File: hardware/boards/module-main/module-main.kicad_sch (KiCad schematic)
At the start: 2 parts, among them J2 2x10 2.54mm pin header, J3 Neutrik NE8FAV

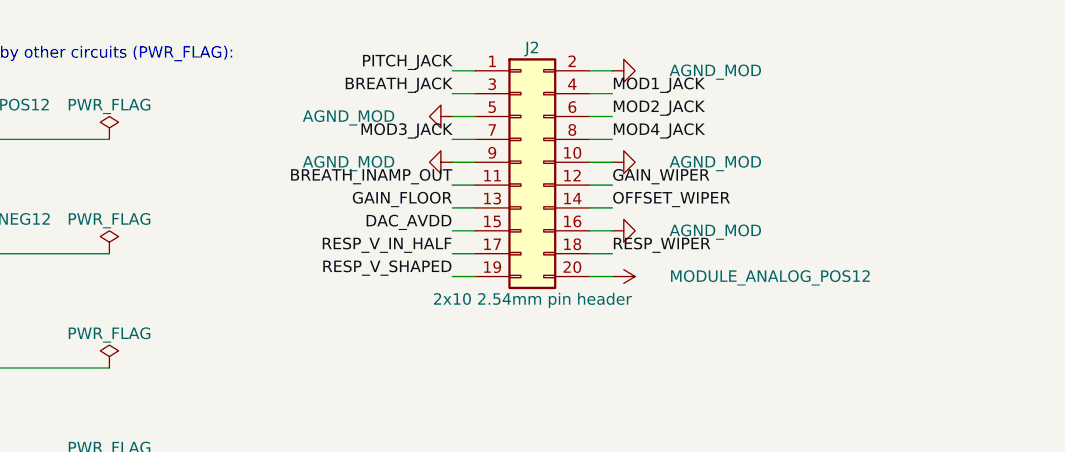
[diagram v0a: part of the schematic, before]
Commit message: Module schematics: the ten circuits' netlists exported from their sheets; J-B2B-MOD allocated by position
- Every module circuit's netlist.yaml is now EXPORTED from its KiCad sheet
  (ADR 0019), identical part by part and net by net to the hand-written one,
  including its foreign: parts. kicad.py exports foreign: from FOREIGN lines of
  sheet text; without it the breath receive page's R1 went unresolved.
- J-B2B-MOD, re-allocated: the pots' nets on the top rows (the pots sit above
  the header), each side's pot and jacks in its own column, a ground on the
  diagonal of every other row so every signal but the LED's +12 V has a ground
  pin beside it.
- kicad.py check: J-B2B-MOD is one conductor per pin on both module boards, and
  the main board's etherCON matches hardware/interfaces/spi-link pin for pin.
- sch.py: a board's sub-sheet pin with one member is a no-connect again (the
  interfaces' spare-label rule assumed a part pin).

Co-Authored-By: Claude Opus 5.5 <noreply@anthropic.com>
Claude-Session: https://claude.ai/code/session_01LmB4muFXnoLprWX4JzuJ5A
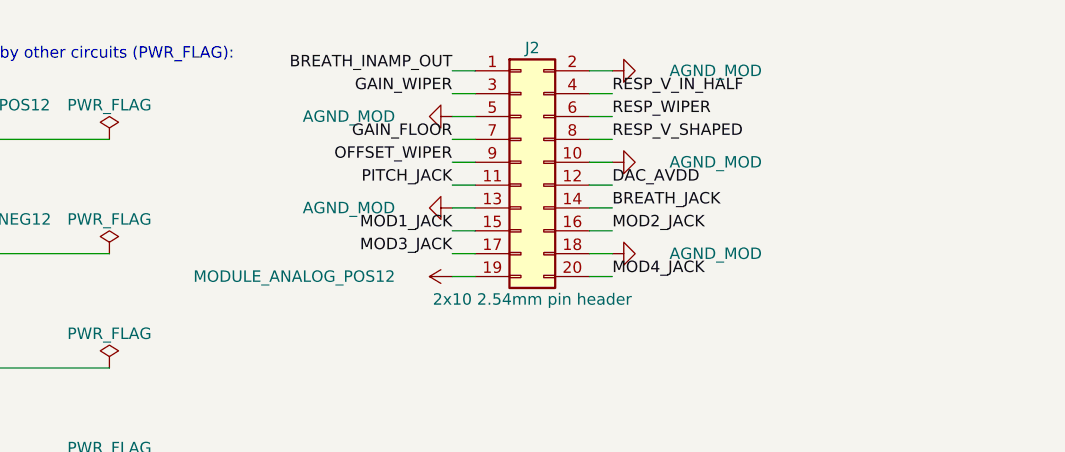
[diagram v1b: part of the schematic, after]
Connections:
- net AGND_MOD: now also J2.13 (Pin_13), J2.18 (Pin_18); no longer J2.16 (Pin_16), J2.9 (Pin_9)
- net BREATH_INAMP_OUT: now also J2.1 (Pin_1); no longer J2.11 (Pin_11)
- net BREATH_JACK: now also J2.14 (Pin_14); no longer J2.3 (Pin_3)
- net DAC_AVDD: now also J2.12 (Pin_12); no longer J2.15 (Pin_15)
- net GAIN_FLOOR: now also J2.7 (Pin_7); no longer J2.13 (Pin_13)
- net GAIN_WIPER: now also J2.3 (Pin_3); no longer J2.12 (Pin_12)
- net MOD1_JACK: now also J2.15 (Pin_15); no longer J2.4 (Pin_4)
- net MOD2_JACK: now also J2.16 (Pin_16); no longer J2.6 (Pin_6)
- net MOD3_JACK: now also J2.17 (Pin_17); no longer J2.7 (Pin_7)
- net MOD4_JACK: now also J2.20 (Pin_20); no longer J2.8 (Pin_8)
- net MODULE_ANALOG_POS12: now also J2.19 (Pin_19); no longer J2.20 (Pin_20)
- net OFFSET_WIPER: now also J2.9 (Pin_9); no longer J2.14 (Pin_14)
- net PITCH_JACK: now also J2.11 (Pin_11); no longer J2.1 (Pin_1)
- net RESP_V_IN_HALF: now also J2.4 (Pin_4); no longer J2.17 (Pin_17)
- net RESP_V_SHAPED: now also J2.8 (Pin_8); no longer J2.19 (Pin_19)
- net RESP_WIPER: now also J2.6 (Pin_6); no longer J2.18 (Pin_18)

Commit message: dac8568: CLR is a net inside the circuit, tied inactive, not a port waiting for an unfitted part
CLR is active low and falling-edge triggered (SBAS430E p.40); R-CLR-PU ties it
to AVDD and LK-CLR asserts it by hand. The hierarchical port, the board's
no-connect sheet pin and the nets.yaml boundary entry are gone. Whether to
restore link supervision is marked as the owner's decision.

Co-Authored-By: Claude Opus 5.5 <noreply@anthropic.com>
Claude-Session: https://claude.ai/code/session_01LmB4muFXnoLprWX4JzuJ5A
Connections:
- no-connect marks 1 -> 0
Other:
- sheet dac8568 ports: added none; removed CLR
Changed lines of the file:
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@@
     (instances (project "module-main" (path "/fc77e9f9-9171-5c83-92ae-8cafe880764e" (reference "#PWR35") (unit 1))))
   )
-  (no_connect (at 457.2 55.88))
   (wire (pts (xy 457.2 58.42) (xy 454.66 58.42)) (stroke (width 0) (type default)))
   (label "SCLK_DAC" (at 454.66 58.42 180) (fields_autoplaced) (effects (font (size 1.27 1.27)) (justify right bottom)))
@@
     (property "Sheetfile" "../../module/dac8568/dac8568.kicad_sch" (at 457.2 73.66 0) (effects (font (size 1.27 1.27)) (justify left top)))
     (pin "DAC_AVDD" input (at 457.2 53.34 180) (effects (font (size 1.27 1.27)) (justify left)))
-    (pin "CLR" input (at 457.2 55.88 180) (effects (font (size 1.27 1.27)) (justify left)))
     (pin "SCLK_DAC" input (at 457.2 58.42 180) (effects (font (size 1.27 1.27)) (justify left)))
     (pin "DIN" input (at 457.2 60.96 180) (effects (font (size 1.27 1.27)) (justify left)))

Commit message: Panel LED hangs on the load switch output: lit = delivering, dark = off or latched
The LED was on the analog +12 V rail, live whenever the rack is, so it could
not show the -1's latch - the one thing it was kept for. The banked LT1641
datasheet shows TIMER and GATE hold no 'latched' level and PWRGD has the wrong
sense; the output does. J-B2B-MOD pin 19 carries UMBILICAL_POS12 on both
boards; nets.yaml and the allocation table follow.

Co-Authored-By: Claude Opus 5.5 <noreply@anthropic.com>
Claude-Session: https://claude.ai/code/session_01LmB4muFXnoLprWX4JzuJ5A
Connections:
- net MODULE_ANALOG_POS12: no longer J2.19 (Pin_19)
- net UMBILICAL_POS12: now also J2.19 (Pin_19)
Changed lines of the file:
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@@
   (label "MOD3_JACK" (at 454.66 165.1 180) (fields_autoplaced) (effects (font (size 1.27 1.27)) (justify right bottom)))
   (wire (pts (xy 101.6 76.2) (xy 99.06 76.2)) (stroke (width 0) (type default)))
-  (symbol (lib_id "power:+12V") (at 99.06 76.2 90) (unit 1)
-    (in_bom yes) (on_board yes) (dnp no)
-    (property "Reference" "#PWR13" (at 102.87 76.2 0) (effects (font (size 1.27 1.27)) hide))
-    (property "Value" "MODULE_ANALOG_POS12" (at 92.71 76.2 90) (effects (font (size 1.27 1.27)) (justify left)))
-    (property "Footprint" "" (at 99.06 76.2 0) (effects (font (size 1.27 1.27)) hide))
-    (property "Datasheet" "" (at 99.06 76.2 0) (effects (font (size 1.27 1.27)) hide))
-    (pin "1")
-    (instances (project "module-main" (path "/fc77e9f9-9171-5c83-92ae-8cafe880764e" (reference "#PWR13") (unit 1))))
-  )
+  (label "UMBILICAL_POS12" (at 99.06 76.2 180) (fields_autoplaced) (effects (font (size 1.27 1.27)) (justify right bottom)))
   (wire (pts (xy 254.0 55.88) (xy 256.54 55.88)) (stroke (width 0) (type default)))
   (symbol (lib_id "power:+12V") (at 256.54 55.88 270) (unit 1)

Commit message: Breath response shaper adopted: restoring half drawn, output feeds POT-GAIN; pots ordered to fit the knob
U-RESP B restores x2 inverting (R-RESTORE-IN 10k, R-RESTORE-FB 20k): unity and
the in-amp's polarity at centre detent. BREATH_SHAPED feeds POT-GAIN on
J-B2B-MOD pin 1; nets.yaml moves the shaper from proposed to fitted.
POT-GAIN linear (the design's working gain sits at noon); POT-OFFSET gets no
detent. POT-GAIN/OFFSET are Song Huei R0904N KC (18-tooth, the T18 knob's
shaft; KQ is 40-tooth); POT-RESP Alpha RV09AF-40-25B-B50K-0C (18-tooth B shaft,
centre click). POT-OFFSET's zero is +18.7 deg on the 280-deg track, not 300.

Co-Authored-By: Claude Opus 5.5 <noreply@anthropic.com>
Claude-Session: https://claude.ai/code/session_01LmB4muFXnoLprWX4JzuJ5A
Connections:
- net BREATH_INAMP_OUT: no longer J2.1 (Pin_1)
- new net BREATH_SHAPED: J2.1 (Pin_1)
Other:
- sheet breath-response-shaper ports: added BREATH_SHAPED; removed none
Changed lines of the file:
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@@
   )
   (wire (pts (xy 101.6 53.34) (xy 99.06 53.34)) (stroke (width 0) (type default)))
-  (label "BREATH_INAMP_OUT" (at 99.06 53.34 180) (fields_autoplaced) (effects (font (size 1.27 1.27)) (justify right bottom)))
+  (label "BREATH_SHAPED" (at 99.06 53.34 180) (fields_autoplaced) (effects (font (size 1.27 1.27)) (justify right bottom)))
   (wire (pts (xy 254.0 96.52) (xy 256.54 96.52)) (stroke (width 0) (type default)))
   (label "BREATH_INAMP_OUT" (at 256.54 96.52 0) (fields_autoplaced) (effects (font (size 1.27 1.27)) (justify left bottom)))
@@
     (pin "MODULE_ANALOG_NEG12" input (at 330.2 147.32 180) (effects (font (size 1.27 1.27)) (justify left)))
     (pin "V_SHAPED" passive (at 330.2 149.86 180) (effects (font (size 1.27 1.27)) (justify left)))
+    (pin "BREATH_SHAPED" output (at 330.2 152.4 180) (effects (font (size 1.27 1.27)) (justify left)))
     (instances (project "module-main" (path "/fc77e9f9-9171-5c83-92ae-8cafe880764e" (page "8"))))
   )
+  (wire (pts (xy 330.2 152.4) (xy 327.66 152.4)) (stroke (width 0) (type default)))
+  (label "BREATH_SHAPED" (at 327.66 152.4 180) (fields_autoplaced) (effects (font (size 1.27 1.27)) (justify right bottom)))
   (sheet (at 203.2 139.7) (size 50.8 20.32) (exclude_from_sim no) (in_bom yes) (on_board yes) (dnp no)
     (stroke (width 0.1524) (type solid)) (fill (color 0 0 0 0.0000))

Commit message: Module: four-layer ground settled, local 5 V, metal standoffs, pitch budget, board-to-board header
Owner decisions of 2026-09-30 applied. dig-gnd-topology settled: one star at
J-PWR-EURO's ground pins, DIG_GND a layer-2 plane tied there by the new
NT-DIG-MOD, AGND_MOD its own region by NT-AGND-MOD, PWR_GND on layer 4; the
proposal's bridge under the DAC dropped per SBAS430E p.49 (DIG_GND was an
island tied only through the cable before). PCB-MODULE four layers, the jack
board two. The bus +5 V is not used: U-REG-LOGIC (ADP7118AUJZ-5.0, banked)
makes LOGIC_5V from the analog +12 V; FB4/C4 gone, the 16-pin header kept
with its +5 V/CV/Gate pins no-connect (ADR 0023 point 3 amended). Metal
standoffs: pads AGND_MOD on the jack board, no net on the main board.
pitch-cents-budget settled at 0.76 cents linear / 0.45 RSS from one table.
J-B2B-MOD is Samtec TSW-110-09-G-D. Module sims are stale and re-run next.

Co-Authored-By: Claude Opus 5.5 <noreply@anthropic.com>
Claude-Session: https://claude.ai/code/session_01LmB4muFXnoLprWX4JzuJ5A
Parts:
- J2: LCSC (none) -> C7366478; MPN (none) -> TSW-110-09-G-D; Manufacturer (none) -> Samtec
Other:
- sheet digital-and-supervision ports: added LOGIC_5V; removed BUS_5V
- sheet power-entry ports: added LOGIC_5V; removed BUS_5V
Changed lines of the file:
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@@
     (property "Note" "Soldered through both module boards, no mated contact (ADR 0023). Its pin k is the same conductor on both boards; tools/kicad.py check holds the two sheets to that. Allocation and reasoning: hardware/boards/module-main/README.md" (at 106.68 63.5 0) (effects (font (size 1.27 1.27)) hide))
     (property "Pins_source" "header position n on pin n, odd/even across the two rows as a 2x10 header numbers them" (at 106.68 63.5 0) (effects (font (size 1.27 1.27)) hide))
-    (property "Manufacturer" "" (at 106.68 63.5 0) (effects (font (size 1.27 1.27)) hide))
-    (property "MPN" "" (at 106.68 63.5 0) (effects (font (size 1.27 1.27)) hide))
-    (property "LCSC" "" (at 106.68 63.5 0) (effects (font (size 1.27 1.27)) hide))
+    (property "Manufacturer" "Samtec" (at 106.68 63.5 0) (effects (font (size 1.27 1.27)) hide))
+    (property "MPN" "TSW-110-09-G-D" (at 106.68 63.5 0) (effects (font (size 1.27 1.27)) hide))
+    (property "LCSC" "C7366478" (at 106.68 63.5 0) (effects (font (size 1.27 1.27)) hide))
     (property "Assembly" "hand" (at 106.68 63.5 0) (effects (font (size 1.27 1.27)) hide))
     (pin "1")
@@
     (in_bom yes) (on_board yes) (dnp no)
     (property "Reference" "#PWR34" (at 252.73 60.96 0) (effects (font (size 1.27 1.27)) hide))
-    (property "Value" "BUS_5V" (at 262.89 60.96 270) (effects (font (size 1.27 1.27)) (justify right)))
+    (property "Value" "LOGIC_5V" (at 262.89 60.96 270) (effects (font (size 1.27 1.27)) (justify right)))
     (property "Footprint" "" (at 256.54 60.96 0) (effects (font (size 1.27 1.27)) hide))
     (property "Datasheet" "" (at 256.54 60.96 0) (effects (font (size 1.27 1.27)) hide))
@@
     (in_bom yes) (on_board yes) (dnp no)
     (property "Reference" "#PWR35" (at 331.47 96.52 0) (effects (font (size 1.27 1.27)) hide))
-    (property "Value" "BUS_5V" (at 321.31 96.52 90) (effects (font (size 1.27 1.27)) (justify left)))
+    (property "Value" "LOGIC_5V" (at 321.31 96.52 90) (effects (font (size 1.27 1.27)) (justify left)))
     (property "Footprint" "" (at 327.66 96.52 0) (effects (font (size 1.27 1.27)) hide))
     (property "Datasheet" "" (at 327.66 96.52 0) (effects (font (size 1.27 1.27)) hide))
@@
     (instances (project "module-main" (path "/fc77e9f9-9171-5c83-92ae-8cafe880764e" (reference "#FLG45") (unit 1))))
   )
-  (symbol (lib_id "power:+5V") (at 43.18 124.46 0) (unit 1)
-    (in_bom yes) (on_board yes) (dnp no)
-    (property "Reference" "#PWR46" (at 43.18 128.27 0) (effects (font (size 1.27 1.27)) hide))
-    (property "Value" "BUS_5V" (at 43.18 120.65 0) (effects (font (size 1.27 1.27))))
-    (property "Footprint" "" (at 43.18 124.46 0) (effects (font (size 1.27 1.27)) hide))
-    (property "Datasheet" "" (at 43.18 124.46 0) (effects (font (size 1.27 1.27)) hide))
-    (pin "1")
-    (instances (project "module-main" (path "/fc77e9f9-9171-5c83-92ae-8cafe880764e" (reference "#PWR46") (unit 1))))
-  )
-  (wire (pts (xy 43.18 124.46) (xy 60.96 124.46)) (stroke (width 0) (type default)))
-  (symbol (lib_id "power:PWR_FLAG") (at 60.96 124.46 0) (unit 1)
-    (in_bom yes) (on_board yes) (dnp no)
-    (property "Reference" "#FLG47" (at 60.96 121.92 0) (effects (font (size 1.27 1.27)) hide))
-    (property "Value" "PWR_FLAG" (at 60.96 120.65 0) (effects (font (size 1.27 1.27))))
-    (property "Footprint" "" (at 60.96 124.46 0) (effects (font (size 1.27 1.27)) hide))
-    (property "Datasheet" "" (at 60.96 124.46 0) (effects (font (size 1.27 1.27)) hide))
-    (pin "1")
-    (instances (project "module-main" (path "/fc77e9f9-9171-5c83-92ae-8cafe880764e" (reference "#FLG47") (unit 1))))
-  )
   (symbol (lib_id "power:+12V") (at 43.18 137.16 0) (unit 1)
     (in_bom yes) (on_board yes) (dnp no)
@@
     (pin "MODULE_ANALOG_POS12" output (at 254.0 55.88 0) (effects (font (size 1.27 1.27)) (justify right)))
     (pin "MODULE_ANALOG_NEG12" output (at 254.0 58.42 0) (effects (font (size 1.27 1.27)) (justify right)))
-    (pin "BUS_5V" output (at 254.0 60.96 0) (effects (font (size 1.27 1.27)) (justify right)))
+    (pin "LOGIC_5V" output (at 254.0 60.96 0) (effects (font (size 1.27 1.27)) (justify right)))
     (pin "DAC_AVDD" output (at 254.0 63.5 0) (effects (font (size 1.27 1.27)) (justify right)))
     (instances (project "module-main" (path "/fc77e9f9-9171-5c83-92ae-8cafe880764e" (page "2"))))
@@
     (pin "MOSI" input (at 330.2 91.44 180) (effects (font (size 1.27 1.27)) (justify left)))
     (pin "CS_MOD" input (at 330.2 93.98 180) (effects (font (size 1.27 1.27)) (justify left)))
-    (pin "BUS_5V" input (at 330.2 96.52 180) (effects (font (size 1.27 1.27)) (justify left)))
+    (pin "LOGIC_5V" input (at 330.2 96.52 180) (effects (font (size 1.27 1.27)) (justify left)))
     (pin "DAC_AVDD" input (at 330.2 99.06 180) (effects (font (size 1.27 1.27)) (justify left)))
     (pin "DIG_GND" passive (at 330.2 101.6 180) (effects (font (size 1.27 1.27)) (justify left)))

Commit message: WIP module power entry: rail PTCs, the instrument's isolated supply (U-ISO), ground split
Sheets, exports, BOM rows, banked datasheets (manifest fragment to follow).
The page drawing, ADR 0027, figures and sims are the next commits.

Co-Authored-By: Claude Opus 5.5 <noreply@anthropic.com>
Claude-Session: https://claude.ai/code/session_01LmB4muFXnoLprWX4JzuJ5A
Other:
- sheet power-entry ports: added ISO_POS12; removed BUS_POS12_RAW
- sheet umbilical-load-switch ports: added ISO_POS12; removed BUS_POS12_RAW
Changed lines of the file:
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@@
     (in_bom yes) (on_board yes) (dnp no)
     (property "Reference" "#PWR26" (at 252.73 53.34 0) (effects (font (size 1.27 1.27)) hide))
-    (property "Value" "BUS_POS12_RAW" (at 262.89 53.34 270) (effects (font (size 1.27 1.27)) (justify right)))
+    (property "Value" "ISO_POS12" (at 262.89 53.34 270) (effects (font (size 1.27 1.27)) (justify right)))
     (property "Footprint" "" (at 256.54 53.34 0) (effects (font (size 1.27 1.27)) hide))
     (property "Datasheet" "" (at 256.54 53.34 0) (effects (font (size 1.27 1.27)) hide))
@@
     (in_bom yes) (on_board yes) (dnp no)
     (property "Reference" "#PWR27" (at 331.47 53.34 0) (effects (font (size 1.27 1.27)) hide))
-    (property "Value" "BUS_POS12_RAW" (at 321.31 53.34 90) (effects (font (size 1.27 1.27)) (justify left)))
+    (property "Value" "ISO_POS12" (at 321.31 53.34 90) (effects (font (size 1.27 1.27)) (justify left)))
     (property "Footprint" "" (at 327.66 53.34 0) (effects (font (size 1.27 1.27)) hide))
     (property "Datasheet" "" (at 327.66 53.34 0) (effects (font (size 1.27 1.27)) hide))
@@
     (in_bom yes) (on_board yes) (dnp no)
     (property "Reference" "#PWR48" (at 43.18 140.97 0) (effects (font (size 1.27 1.27)) hide))
-    (property "Value" "BUS_POS12_RAW" (at 43.18 133.35 0) (effects (font (size 1.27 1.27))))
+    (property "Value" "ISO_POS12" (at 43.18 133.35 0) (effects (font (size 1.27 1.27))))
     (property "Footprint" "" (at 43.18 137.16 0) (effects (font (size 1.27 1.27)) hide))
     (property "Datasheet" "" (at 43.18 137.16 0) (effects (font (size 1.27 1.27)) hide))
@@
     (pin "DIG_GND" passive (at 203.2 55.88 180) (effects (font (size 1.27 1.27)) (justify left)))
     (pin "PWR_GND" passive (at 203.2 58.42 180) (effects (font (size 1.27 1.27)) (justify left)))
-    (pin "BUS_POS12_RAW" output (at 254.0 53.34 0) (effects (font (size 1.27 1.27)) (justify right)))
+    (pin "ISO_POS12" output (at 254.0 53.34 0) (effects (font (size 1.27 1.27)) (justify right)))
     (pin "MODULE_ANALOG_POS12" output (at 254.0 55.88 0) (effects (font (size 1.27 1.27)) (justify right)))
     (pin "MODULE_ANALOG_NEG12" output (at 254.0 58.42 0) (effects (font (size 1.27 1.27)) (justify right)))
@@
     (property "Sheetname" "umbilical-load-switch" (at 330.2 49.53 0) (effects (font (size 1.27 1.27)) (justify left bottom)))
     (property "Sheetfile" "../../module/umbilical-load-switch/umbilical-load-switch.kicad_sch" (at 330.2 60.96 0) (effects (font (size 1.27 1.27)) (justify left top)))
-    (pin "BUS_POS12_RAW" input (at 330.2 53.34 180) (effects (font (size 1.27 1.27)) (justify left)))
+    (pin "ISO_POS12" input (at 330.2 53.34 180) (effects (font (size 1.27 1.27)) (justify left)))
     (pin "PWR_GND" passive (at 330.2 55.88 180) (effects (font (size 1.27 1.27)) (justify left)))
     (pin "UMBILICAL_POS12" output (at 381.0 53.34 0) (effects (font (size 1.27 1.27)) (justify right)))

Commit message: Module: rebuild the CAD outputs and swap J-B2B-MOD's jack pins with the jacks
J-B2B-MOD now carries BREATH_JACK on pin 11 and PITCH_JACK on 14, MOD2_JACK on
17 and MOD3_JACK on 16, on both boards' sheets, so each jack's tip still lands
on its own column's side of the header. Exports, renders and SHEETS.csv
regenerated. Every module CAD output rebuilt except the three Blender photos.

Co-Authored-By: Claude Opus 5.5 <noreply@anthropic.com>
Claude-Session: https://claude.ai/code/session_01LmB4muFXnoLprWX4JzuJ5A
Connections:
- net BREATH_JACK: now also J2.11 (Pin_11); no longer J2.14 (Pin_14)
- net MOD2_JACK: now also J2.17 (Pin_17); no longer J2.16 (Pin_16)
- net MOD3_JACK: now also J2.16 (Pin_16); no longer J2.17 (Pin_17)
- net PITCH_JACK: now also J2.14 (Pin_14); no longer J2.11 (Pin_11)
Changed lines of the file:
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@@
   (label "OFFSET_WIPER" (at 454.66 106.68 180) (fields_autoplaced) (effects (font (size 1.27 1.27)) (justify right bottom)))
   (wire (pts (xy 101.6 66.04) (xy 99.06 66.04)) (stroke (width 0) (type default)))
-  (label "PITCH_JACK" (at 99.06 66.04 180) (fields_autoplaced) (effects (font (size 1.27 1.27)) (justify right bottom)))
+  (label "BREATH_JACK" (at 99.06 66.04 180) (fields_autoplaced) (effects (font (size 1.27 1.27)) (justify right bottom)))
   (wire (pts (xy 203.2 147.32) (xy 200.66 147.32)) (stroke (width 0) (type default)))
   (label "PITCH_JACK" (at 200.66 147.32 180) (fields_autoplaced) (effects (font (size 1.27 1.27)) (justify right bottom)))
@@
   (label "DAC_AVDD" (at 200.66 101.6 180) (fields_autoplaced) (effects (font (size 1.27 1.27)) (justify right bottom)))
   (wire (pts (xy 114.3 68.58) (xy 116.84 68.58)) (stroke (width 0) (type default)))
-  (label "BREATH_JACK" (at 116.84 68.58 0) (fields_autoplaced) (effects (font (size 1.27 1.27)) (justify left bottom)))
+  (label "PITCH_JACK" (at 116.84 68.58 0) (fields_autoplaced) (effects (font (size 1.27 1.27)) (justify left bottom)))
   (wire (pts (xy 457.2 114.3) (xy 454.66 114.3)) (stroke (width 0) (type default)))
   (label "BREATH_JACK" (at 454.66 114.3 180) (fields_autoplaced) (effects (font (size 1.27 1.27)) (justify right bottom)))
@@
   (label "MOD1_JACK" (at 454.66 154.94 180) (fields_autoplaced) (effects (font (size 1.27 1.27)) (justify right bottom)))
   (wire (pts (xy 114.3 71.12) (xy 116.84 71.12)) (stroke (width 0) (type default)))
-  (label "MOD2_JACK" (at 116.84 71.12 0) (fields_autoplaced) (effects (font (size 1.27 1.27)) (justify left bottom)))
+  (label "MOD3_JACK" (at 116.84 71.12 0) (fields_autoplaced) (effects (font (size 1.27 1.27)) (justify left bottom)))
   (wire (pts (xy 457.2 160.02) (xy 454.66 160.02)) (stroke (width 0) (type default)))
   (label "MOD2_JACK" (at 454.66 160.02 180) (fields_autoplaced) (effects (font (size 1.27 1.27)) (justify right bottom)))
   (wire (pts (xy 101.6 73.66) (xy 99.06 73.66)) (stroke (width 0) (type default)))
-  (label "MOD3_JACK" (at 99.06 73.66 180) (fields_autoplaced) (effects (font (size 1.27 1.27)) (justify right bottom)))
+  (label "MOD2_JACK" (at 99.06 73.66 180) (fields_autoplaced) (effects (font (size 1.27 1.27)) (justify right bottom)))
   (wire (pts (xy 457.2 165.1) (xy 454.66 165.1)) (stroke (width 0) (type default)))
   (label "MOD3_JACK" (at 454.66 165.1 180) (fields_autoplaced) (effects (font (size 1.27 1.27)) (justify right bottom)))
